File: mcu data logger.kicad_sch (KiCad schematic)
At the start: 25 parts, among them U1 24LC1025, U2 24LC1025, U3 ATMEGA328P-AU, U4 DS1337S_, Y1 Crystal, Y2 Crystal

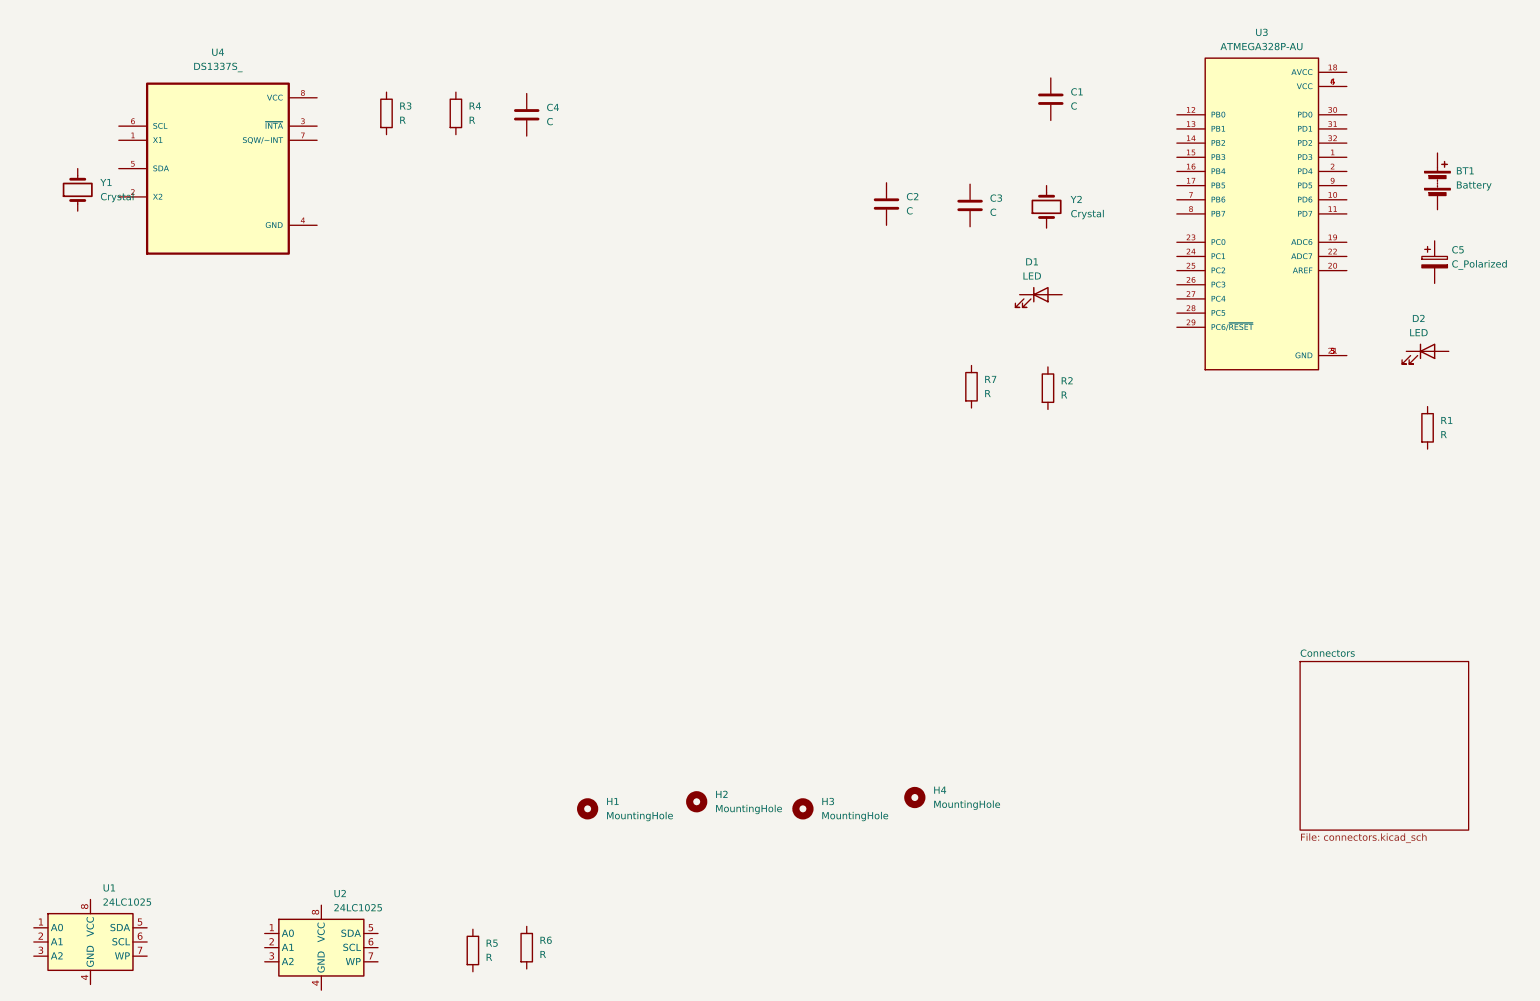
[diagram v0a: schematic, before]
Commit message: Added component values
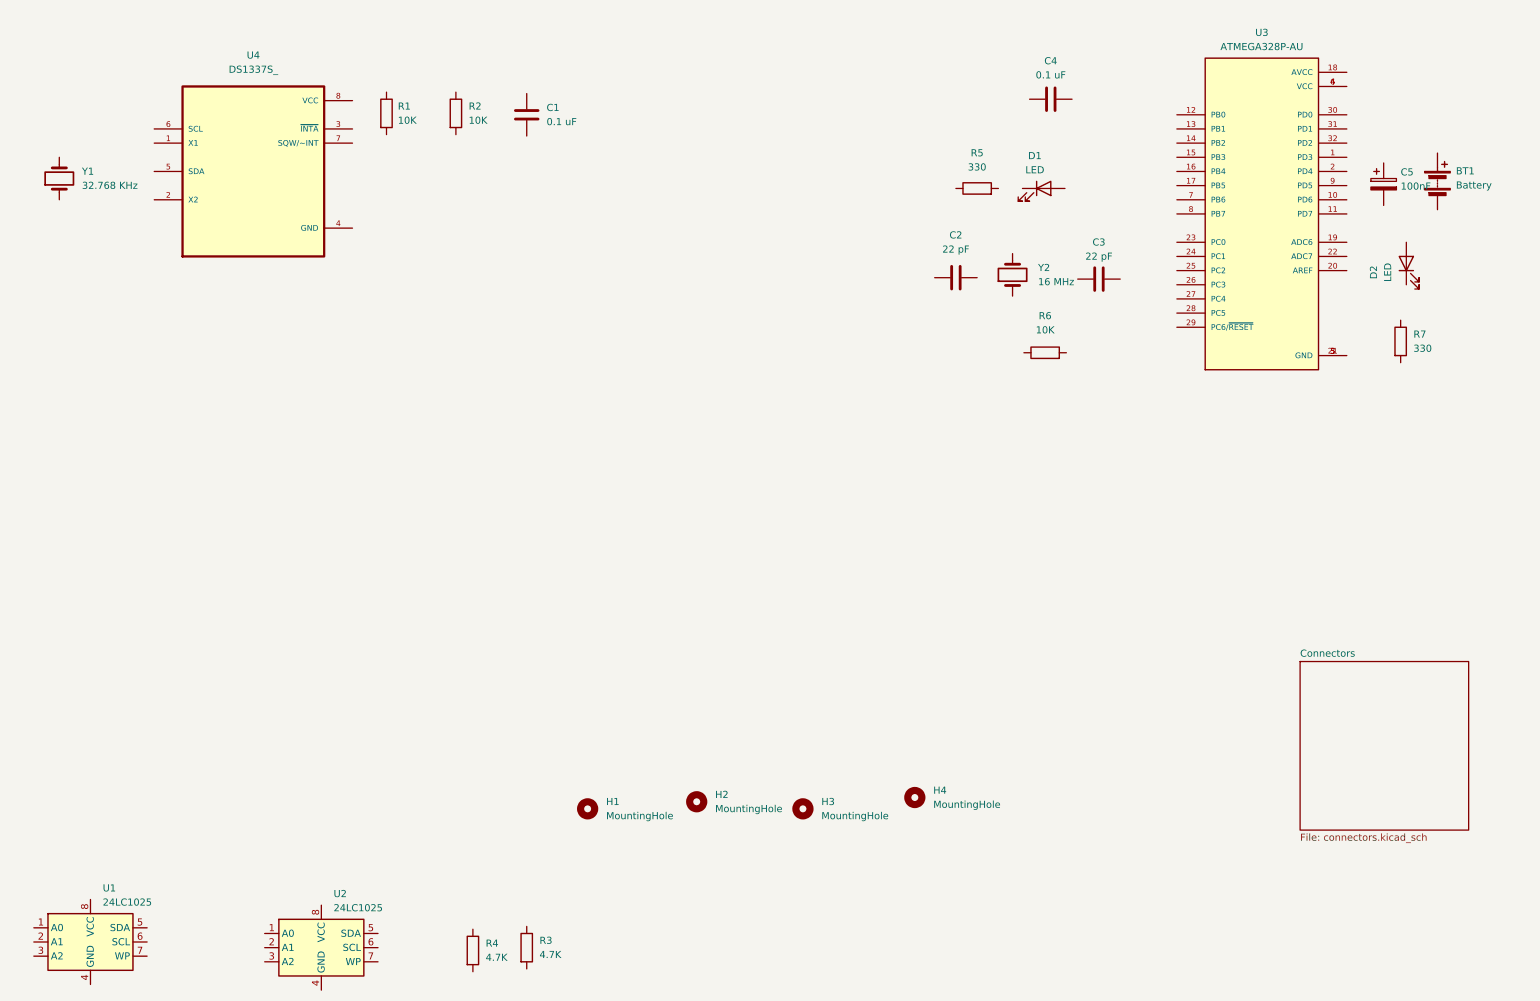
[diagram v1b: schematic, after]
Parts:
- C1: renamed from C4; value C -> 0.1 uF
- C2: renamed from C3; value C -> 22 pF
- C3: renamed from C2; value C -> 22 pF
- C4: renamed from C1; value C -> 0.1 uF
- C5: value C_Polarized -> 100nF
- R1: renamed from R3; value R -> 10K
- R2: renamed from R4; value R -> 10K
- R3: renamed from R6; value R -> 4.7K
- R4: renamed from R5; value R -> 4.7K
- R5: renamed from R7; value R -> 330
- R6: renamed from R2; value R -> 10K
- R7: renamed from R1; value R -> 330
- Y1: value Crystal -> 32.768 KHz
- Y2: value Crystal -> 16 MHz
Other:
- moved on the sheet: C2, C3, C4, C5, D1, D2, R5, R6, R7, U4, Y1, Y2

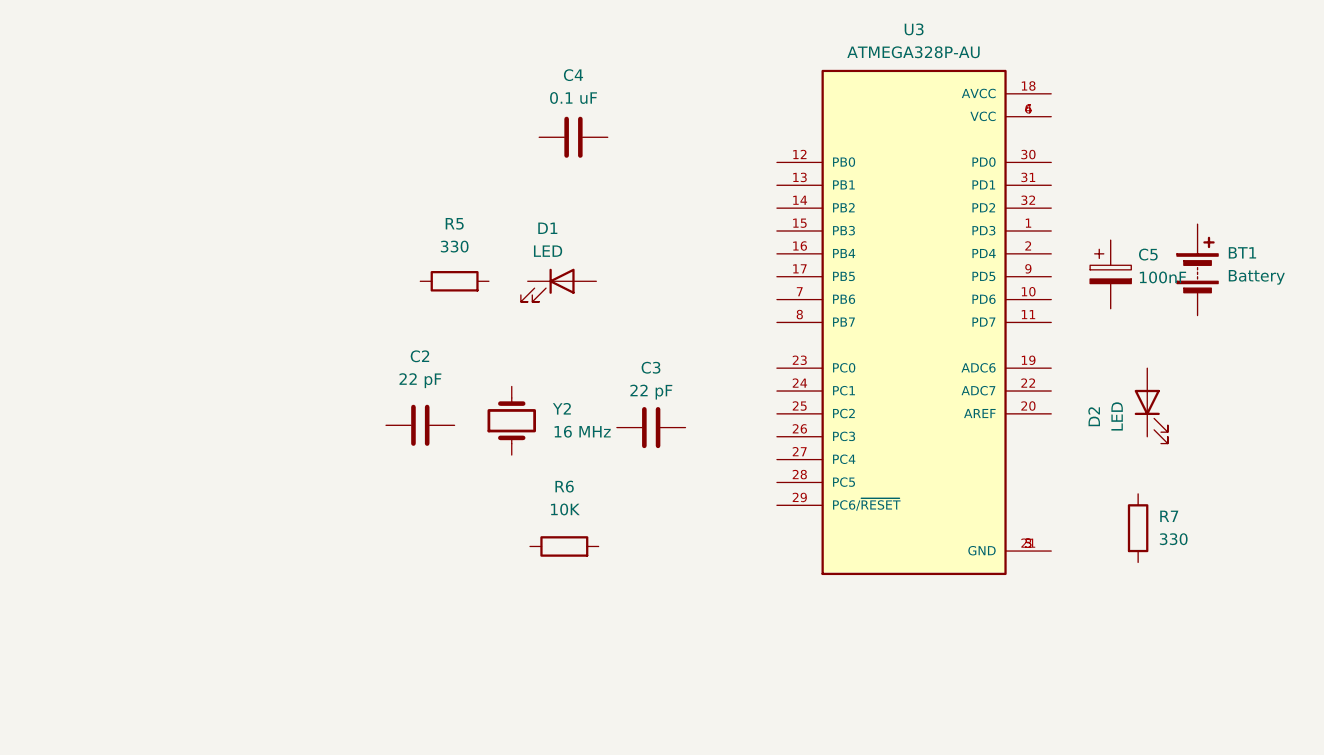
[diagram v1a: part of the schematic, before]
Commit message: completed symbol footprint associations
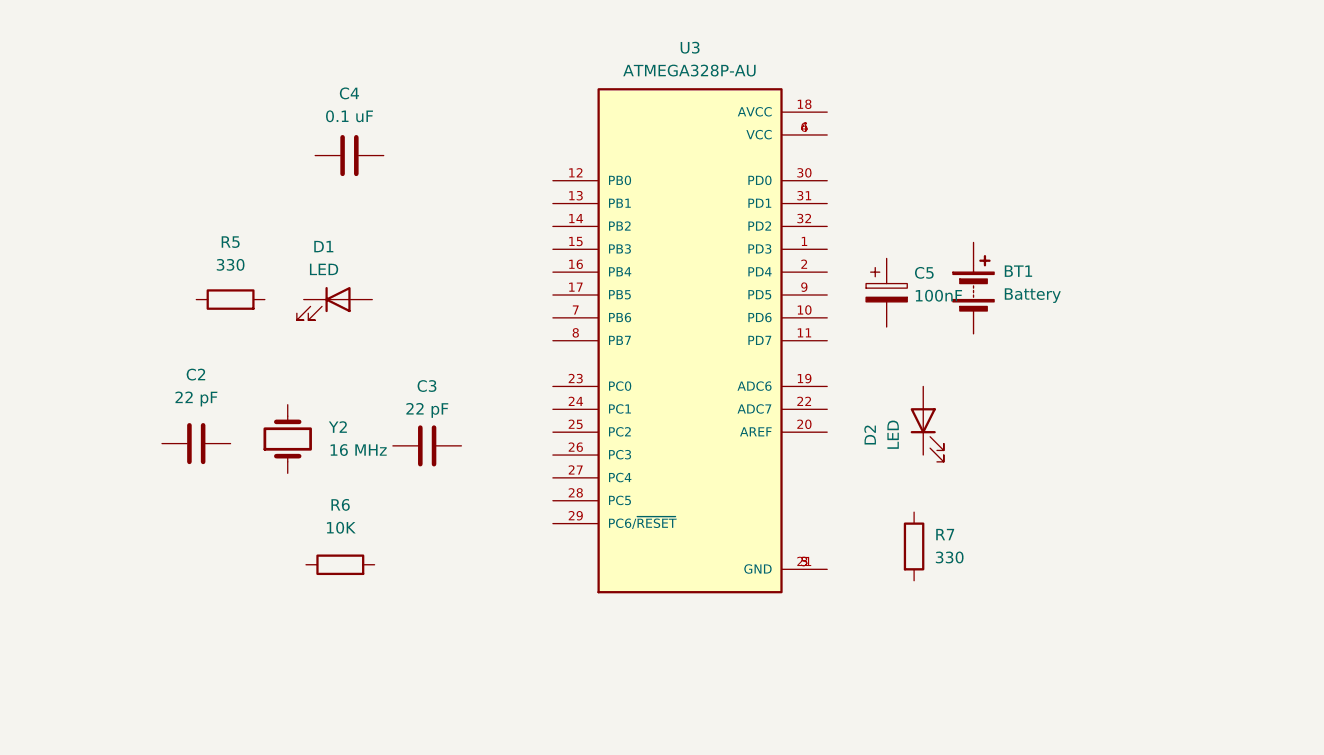
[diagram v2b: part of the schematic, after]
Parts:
- BT1: footprint (none) -> Connector_PinHeader_2.54mm:PinHeader_1x02_P2.54mm_Vertical
- C1, C2, C3, C4, C5: footprint (none) -> Capacitor_SMD:C_0805_2012Metric
- D1, D2: footprint (none) -> LED_SMD:LED_0805_2012Metric
- H1, H2, H3, H4: footprint (none) -> MountingHole:MountingHole_2.1mm
- R1, R2, R3, R4, R5, R6, R7: footprint (none) -> Resistor_SMD:R_0805_2012Metric
- U1, U2: footprint (none) -> Package_SO:SOIC-8_5.23x5.23mm_P1.27mm
- Y1, Y2: footprint (none) -> Crystal:Crystal_SMD_5032-2Pin_5.0x3.2mm_HandSoldering
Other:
- moved on the sheet: BT1, C2, C3, C4, C5, D1, D2, R5, R6, R7, U3, Y2

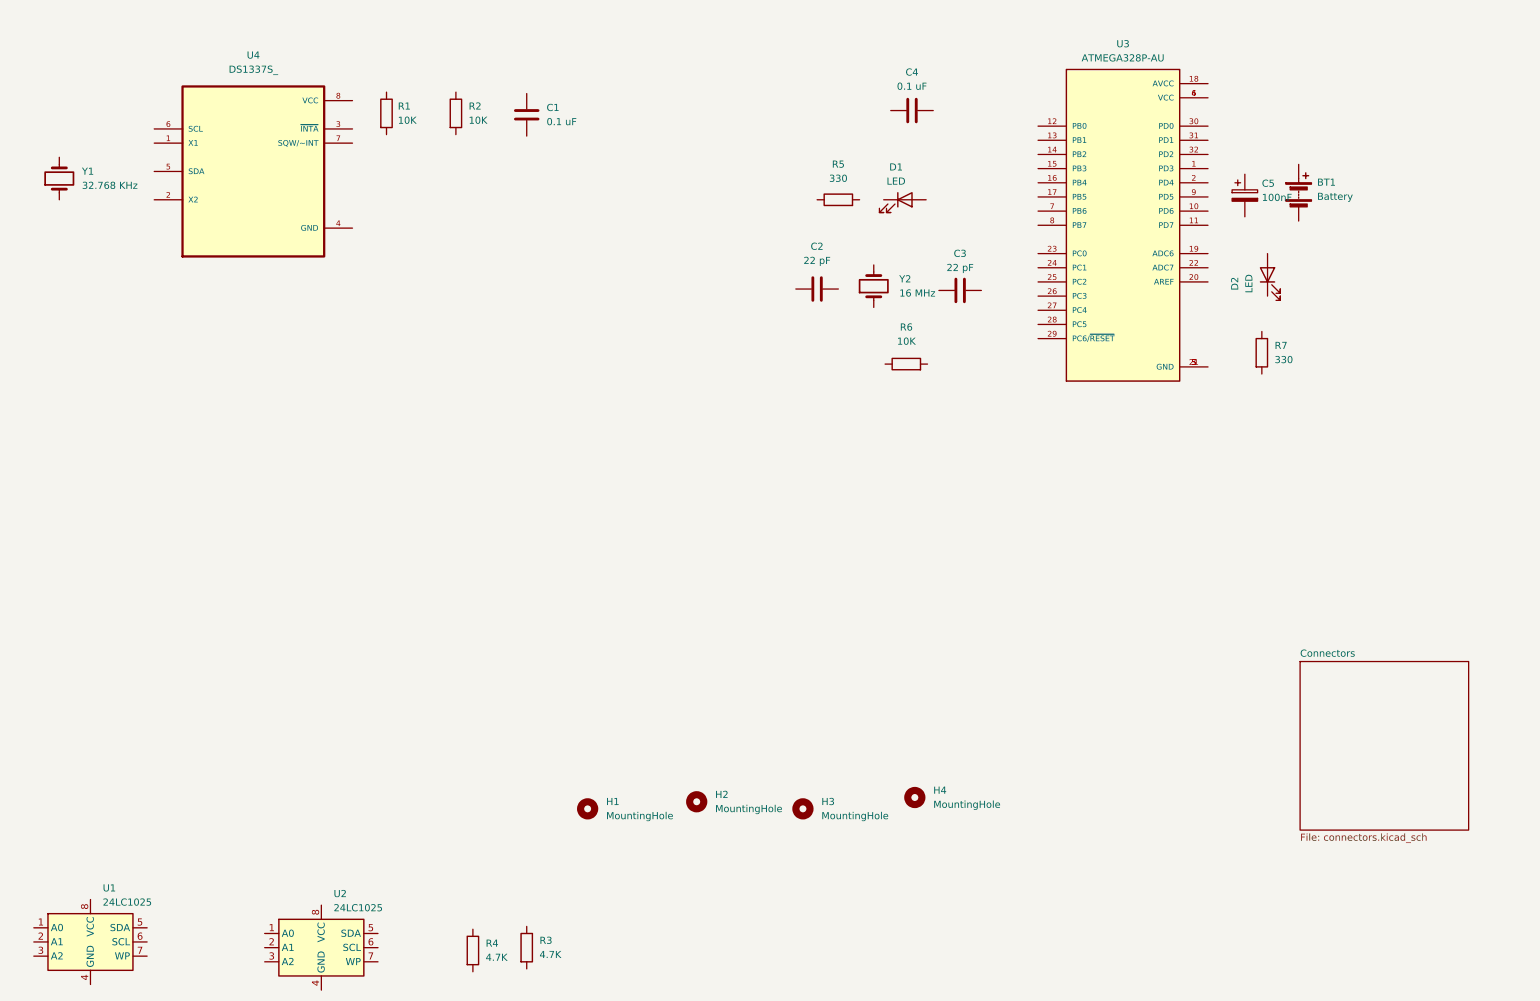
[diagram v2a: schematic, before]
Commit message: Completed wiring of main sheet
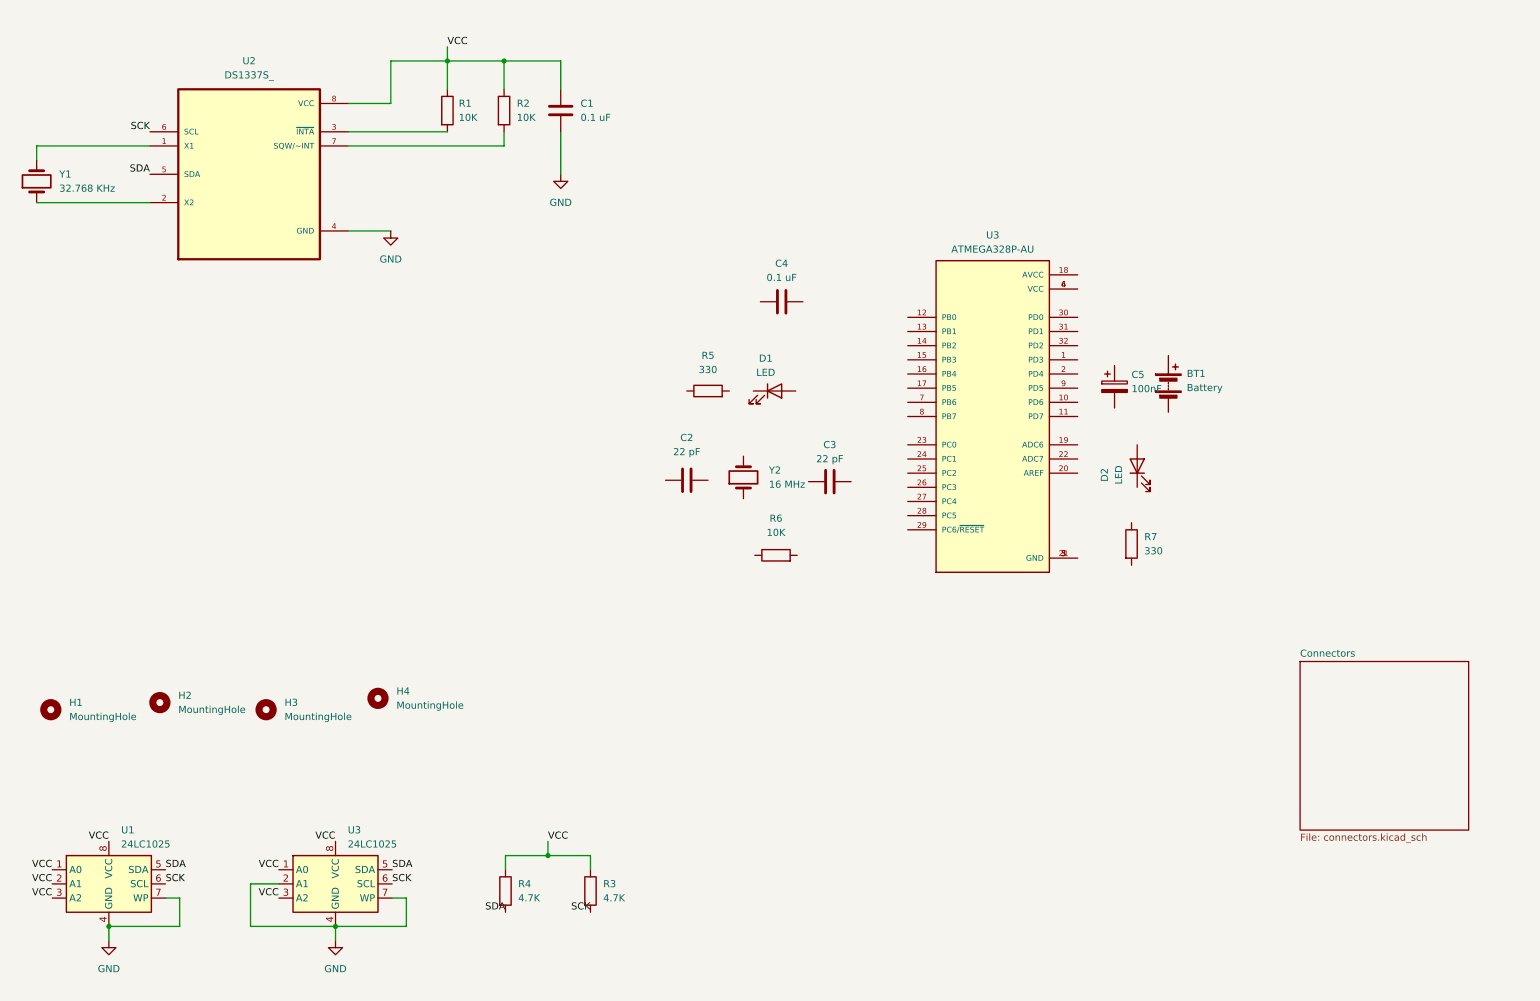
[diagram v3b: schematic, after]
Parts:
- renumbered U4 to U2, U2 to U3
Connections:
- net at Y1.1: now also U2.2 (X2)
- net at Y1.2: now also U2.1 (X1)
- net VCC: now reaches R2.1
- net VCC: now also C1.1, R1.1, R3.1, R4.1, U1.1 (A0), U1.2 (A1), U1.3 (A2), U1.8 (VCC), U2.8 (VCC), U3.1 (A0), U3.3 (A2), U3.8 (VCC)
- net at R2.2: now also U2.7 (SQW/~INT)
- net GND: now reaches C1.2
- net GND: now also U1.4 (GND), U1.7 (WP), U2.4 (GND), U3.2 (A1), U3.4 (GND), U3.7 (WP)
- net SDA: now reaches R4.2
- net SDA: now also U1.5 (SDA), U2.5 (SDA), U3.5 (SDA)
- net SCK: now reaches R3.2
- net SCK: now also U1.6 (SCL), U2.6 (SCL), U3.6 (SCL)
- net at R1.2: now also U2.3 (~{INTA})
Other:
- moved on the sheet: BT1, C1, C2, C3, C4, C5, D1, D2, H1, H2, H3, H4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

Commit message: completed wiring in the schemeatic
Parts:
- U4: renamed from U3; footprint ATMEGA328P-AU:QFP80P900X900X120-32N -> (none); Check_prices https://www.snapeda.com/parts/ATMEGA328P-AU/Microchip/view-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 -> (none); Purchase-URL https://www.snapeda.com/api/url_track_click_mouser/?unipart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 -> (none); SnapEDA_Link https://www.snapeda.com/parts/ATMEGA328P-AU/Microchip/view-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 -> (none)
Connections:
- net GND: now also BT1.2 (-), C2.2, C3.2, C4.1, C5.2, R5.1, R7.2, U4.21 (GND), U4.3 (GND), U4.5 (GND)
- net SCK: now also D1.2 (A), U4.17 (PB5), U4.28 (PC5)
- net SDA: now also U4.27 (PC4)
- net VCC: now also R6.1
- net at BT1.1 (+): now also C5.1, D2.2 (A), U4.18 (AVCC), U4.4 (VCC)
- net at R7.1: now also D2.1 (K)
- net at C2.1: now also U4.7 (PB6), Y2.2
- net D3: now reaches U4.1 (PD3)
- net D6: now reaches U4.10 (PD6)
- net D7: now reaches U4.11 (PD7)
- net D8: now reaches U4.12 (PB0)
- net MOSI: now reaches U4.15 (PB3)
- net MISO: now reaches U4.16 (PB4)
- net D4: now reaches U4.2 (PD4)
- net at U4.20 (AREF): now also C4.2
- net RESET: now reaches U4.29 (PC6/~{RESET})
- net RESET: now also R6.2
- net RX: now reaches U4.30 (PD0)
- net TX: now reaches U4.31 (PD1)
- net D2: now reaches U4.32 (PD2)
- net at U4.6 (VCC): no longer U4.4 (VCC)
- net at U4.8 (PB7): now also C3.1, Y2.1
- net D5: now reaches U4.9 (PD5)
- net at R5.2: now also D1.1 (K)
- no-connect marks 0 -> 9
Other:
- sheet Connectors ports: added D2, D3, D4, D5, D6, D7, D8, GND, MISO, MOSI, RESET, RX, SCK, SDA, TX, VCC; removed none
- moved on the sheet: BT1, C2, C3, C4, C5, D1, D2, H1, H2, H3, H4, R3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
